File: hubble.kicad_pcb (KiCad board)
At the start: 4 copper layers, 60 x 80 mm, 97 parts, among them J1 USB3_A_LCSC, J2 USB3_A_LCSC, J3 USB_C_Receptacle_Molex, J5 USB3_A_LCSC, J6 USB3_A_LCSC, J7 USB3_A_LCSC, J8 USB3_A_LCSC, J9 Conn_02x02_Odd_Even, SW1 K3-2235D-F1, U1 MAX6816EUS+T, U10 TPD1E05U06DPY, U11 TPD1E05U06DPY, U12 TPD1E05U06DPY, U13 TPD1E05U06DPY, U2 TPD1E05U06DPY, U3 TS3USB221RSER, U4 TPS7A5201QRGRRQ1, U5 USB5744, U6 TPS7A5201QRGRRQ1, U7 FUSB340, U8 TPD1E05U06DPY, U9 TPD1E05U06DPY, Y1 X322525MOB4SI

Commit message: Add ki-lime-pi-to-go submodule, upgrade to KiCad 9, put a Pico W and through hole header on the schematic
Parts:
- added A1: RaspberryPi_Pico_W, Module_RaspberryPi_Pico:RaspberryPi_Pico_Common_THT, F.Cu at (70.1, 74.4)
- added J10: Pico_Socket_B, Module_RaspberryPi_Pico:RaspberryPi_Pico_PinSocket_1x20_P2.54mm_Vertical, F.Cu at (97.0, 97.5)
- added J4: Pico_Socket_A, Module_RaspberryPi_Pico:RaspberryPi_Pico_PinSocket_1x20_P2.54mm_Vertical, F.Cu at (35.9, 51.1)

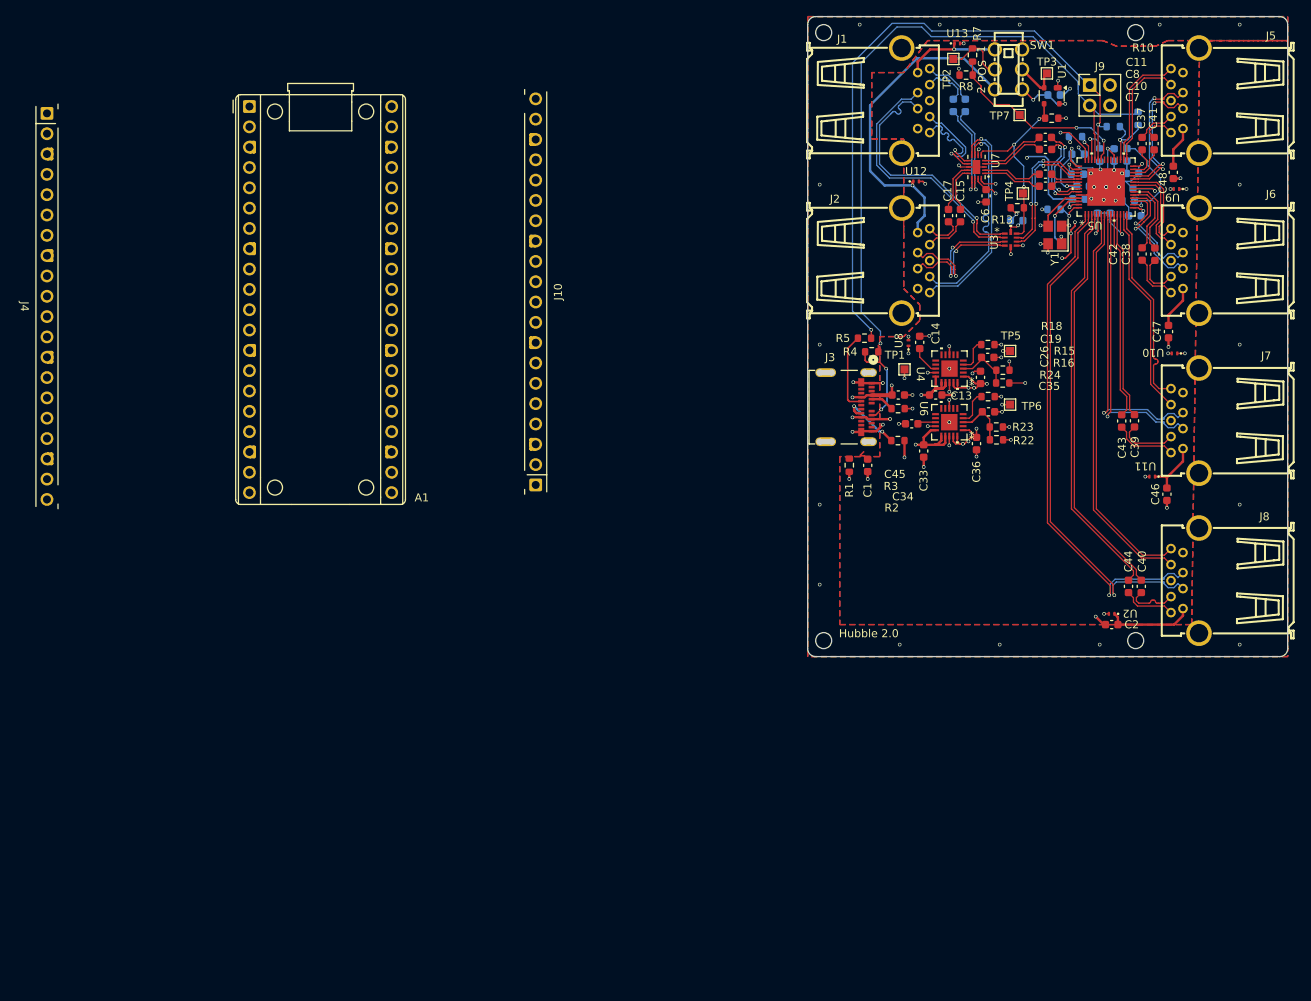
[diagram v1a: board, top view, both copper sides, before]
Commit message: Start wiring up Pi Pico
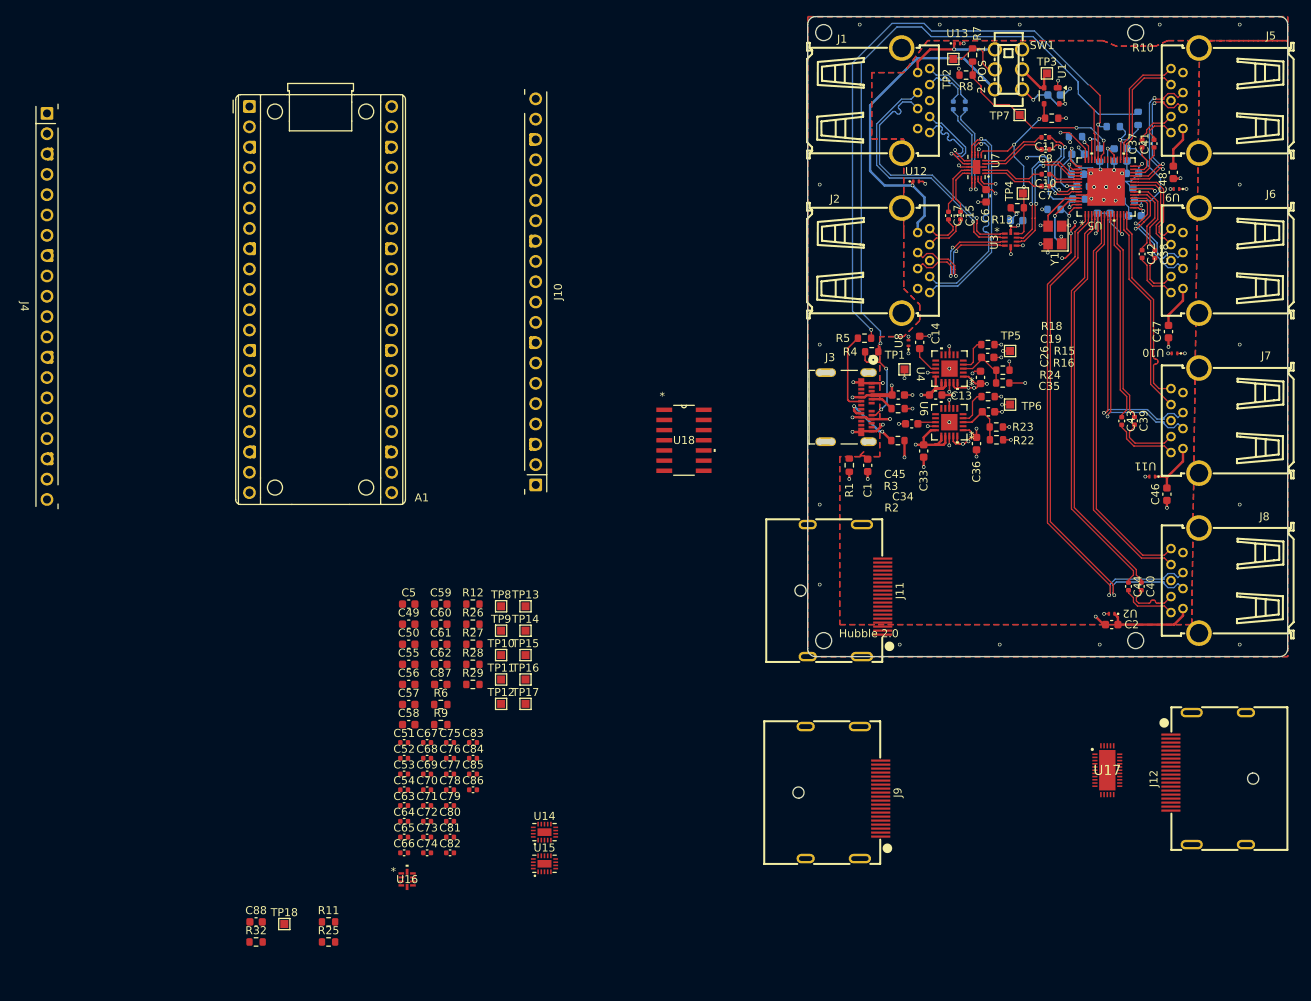
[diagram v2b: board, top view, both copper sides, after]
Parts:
- added C49: 0.1uF, Capacitor_SMD:C_0603_1608Metric, F.Cu at (81.1, 115.0)
- added C5: 0.1uF, Capacitor_SMD:C_0603_1608Metric, F.Cu at (81.1, 112.4)
- added C50: 0.1uF, Capacitor_SMD:C_0603_1608Metric, F.Cu at (81.1, 117.5)
- added C51: 0.1uF, Capacitor_SMD:C_0402_1005Metric, F.Cu at (80.6, 129.7)
- added C52: 0.1uF, Capacitor_SMD:C_0402_1005Metric, F.Cu at (80.6, 131.7)
- added C53: 0.1uF, Capacitor_SMD:C_0402_1005Metric, F.Cu at (80.6, 133.7)
- added C54: 0.1uF, Capacitor_SMD:C_0402_1005Metric, F.Cu at (80.6, 135.7)
- added C55: 0.1uF, Capacitor_SMD:C_0603_1608Metric, F.Cu at (81.1, 120.0)
- added C56: 0.1uF, Capacitor_SMD:C_0603_1608Metric, F.Cu at (81.1, 122.5)
- added C57: 0.1uF, Capacitor_SMD:C_0603_1608Metric, F.Cu at (81.1, 125.0)
- added C58: 0.1uF, Capacitor_SMD:C_0603_1608Metric, F.Cu at (81.1, 127.5)
- added C59: 0.1uF, Capacitor_SMD:C_0603_1608Metric, F.Cu at (85.1, 112.4)
- added C60: 0.1uF, Capacitor_SMD:C_0603_1608Metric, F.Cu at (85.1, 115.0)
- added C61: 0.1uF, Capacitor_SMD:C_0603_1608Metric, F.Cu at (85.1, 117.5)
- added C62: 4.7uF, Capacitor_SMD:C_0603_1608Metric, F.Cu at (85.1, 120.0)
- added C63: 0.1uF, Capacitor_SMD:C_0402_1005Metric, F.Cu at (80.6, 137.6)
- added C64: 0.1uF, Capacitor_SMD:C_0402_1005Metric, F.Cu at (80.6, 139.6)
- added C65: 0.1uF, Capacitor_SMD:C_0402_1005Metric, F.Cu at (80.6, 141.6)
- added C66: 0.1uF, Capacitor_SMD:C_0402_1005Metric, F.Cu at (80.6, 143.5)
- added C67: 0.1uF, Capacitor_SMD:C_0402_1005Metric, F.Cu at (83.4, 129.7)
- added C68: 0.1uF, Capacitor_SMD:C_0402_1005Metric, F.Cu at (83.4, 131.7)
- added C69: 0.1uF, Capacitor_SMD:C_0402_1005Metric, F.Cu at (83.4, 133.7)
- added C70: 0.1uF, Capacitor_SMD:C_0402_1005Metric, F.Cu at (83.4, 135.7)
- added C71: 0.1uF, Capacitor_SMD:C_0402_1005Metric, F.Cu at (83.4, 137.6)
- added C72: 0.1uF, Capacitor_SMD:C_0402_1005Metric, F.Cu at (83.4, 139.6)
- added C73: 0.1uF, Capacitor_SMD:C_0402_1005Metric, F.Cu at (83.4, 141.6)
- added C74: 0.1uF, Capacitor_SMD:C_0402_1005Metric, F.Cu at (83.4, 143.5)
- added C75: 0.1uF, Capacitor_SMD:C_0402_1005Metric, F.Cu at (86.3, 129.7)
- added C76: 0.1uF, Capacitor_SMD:C_0402_1005Metric, F.Cu at (86.3, 131.7)
- added C77: 0.1uF, Capacitor_SMD:C_0402_1005Metric, F.Cu at (86.3, 133.7)
- added C78: 0.1uF, Capacitor_SMD:C_0402_1005Metric, F.Cu at (86.3, 135.7)
- added C79: 0.1uF, Capacitor_SMD:C_0402_1005Metric, F.Cu at (86.3, 137.6)
- added C80: 0.1uF, Capacitor_SMD:C_0402_1005Metric, F.Cu at (86.3, 139.6)
- added C81: 0.1uF, Capacitor_SMD:C_0402_1005Metric, F.Cu at (86.3, 141.6)
- added C82: 0.1uF, Capacitor_SMD:C_0402_1005Metric, F.Cu at (86.3, 143.5)
- added C83: 0.1uF, Capacitor_SMD:C_0402_1005Metric, F.Cu at (89.2, 129.7)
- added C84: 0.1uF, Capacitor_SMD:C_0402_1005Metric, F.Cu at (89.2, 131.7)
- added C85: 0.1uF, Capacitor_SMD:C_0402_1005Metric, F.Cu at (89.2, 133.7)
- added C86: 0.1uF, Capacitor_SMD:C_0402_1005Metric, F.Cu at (89.2, 135.7)
- added C87: 0.1uF, Capacitor_SMD:C_0603_1608Metric, F.Cu at (85.1, 122.5)
- added C88: 0.1uF, Capacitor_SMD:C_0603_1608Metric, F.Cu at (62.0, 152.2)
- added J11: DisplayPort, hubble:DISPLAYPORT_XDPF-0205-20S, F.Cu at (135.7, 110.8)
- added J12: DisplayPort, hubble:DISPLAYPORT_XDPF-0205-20S, F.Cu at (181.1, 134.2)
- added R11: 0, Resistor_SMD:R_0603_1608Metric, F.Cu at (71.1, 152.2)
- added R12: 1M, Resistor_SMD:R_0603_1608Metric, F.Cu at (89.1, 112.4)
- added R25: 0, Resistor_SMD:R_0603_1608Metric, F.Cu at (71.1, 154.7)
- added R26: 10k, Resistor_SMD:R_0603_1608Metric, F.Cu at (89.1, 115.0)
- added R27: 10k, Resistor_SMD:R_0603_1608Metric, F.Cu at (89.1, 117.5)
- added R28: 1M, Resistor_SMD:R_0603_1608Metric, F.Cu at (89.1, 120.0)
- added R29: 330, Resistor_SMD:R_0603_1608Metric, F.Cu at (89.1, 122.5)
- added R32: 10k, Resistor_SMD:R_0603_1608Metric, F.Cu at (62.0, 154.7)
- added R6: 330, Resistor_SMD:R_0603_1608Metric, F.Cu at (85.1, 125.0)
- added R9: 330, Resistor_SMD:R_0603_1608Metric, F.Cu at (85.1, 127.5)
- added TP10: TestPoint, TestPoint:TestPoint_Pad_1.0x1.0mm, F.Cu at (92.7, 118.8)
- added TP11: TestPoint, TestPoint:TestPoint_Pad_1.0x1.0mm, F.Cu at (92.7, 121.9)
- added TP12: TestPoint, TestPoint:TestPoint_Pad_1.0x1.0mm, F.Cu at (92.7, 124.9)
- added TP13: TestPoint, TestPoint:TestPoint_Pad_1.0x1.0mm, F.Cu at (95.7, 112.7)
- added TP14: TestPoint, TestPoint:TestPoint_Pad_1.0x1.0mm, F.Cu at (95.7, 115.8)
- added TP15: TestPoint, TestPoint:TestPoint_Pad_1.0x1.0mm, F.Cu at (95.7, 118.8)
- added TP16: TestPoint, TestPoint:TestPoint_Pad_1.0x1.0mm, F.Cu at (95.7, 121.9)
- added TP17: TestPoint, TestPoint:TestPoint_Pad_1.0x1.0mm, F.Cu at (95.7, 124.9)
- added TP18: TestPoint, TestPoint:TestPoint_Pad_1.0x1.0mm, F.Cu at (65.6, 152.4)
- added TP8: TestPoint, TestPoint:TestPoint_Pad_1.0x1.0mm, F.Cu at (92.7, 112.7)
- added TP9: TestPoint, TestPoint:TestPoint_Pad_1.0x1.0mm, F.Cu at (92.7, 115.8)
- added U14: FUSB340, hubble:TMLP-18_L2.8-W2.0-P0.40-BL-EP, F.Cu at (98.1, 140.9)
- added U15: FUSB340, hubble:TMLP-18_L2.8-W2.0-P0.40-BL-EP, F.Cu at (98.1, 144.9)
- added U16: TS3USB221RSER, hubble:UQFN-10, F.Cu at (80.9, 146.9)
- added U17: PI3DPX1203BZLEX, hubble:QFN40P300X600X80-33N, F.Cu at (168.4, 133.2)
- added U18: SN74CBTLV3126DR, hubble:D14, F.Cu at (115.5, 92.0)
- C10, C11, C15, C16, C17, C18, C37, C38, C39, C40, C41, C42, C43, C44, C7, C8: footprint Capacitor_SMD:C_0603_1608Metric -> Capacitor_SMD:C_0402_1005Metric
- J9: value Conn_02x02_Odd_Even -> DisplayPort; footprint Connector_PinHeader_2.54mm:PinHeader_2x02_P2.54mm_Vertical -> hubble:DISPLAYPORT_XDPF-0205-20S
- moved J9 93.7 mm to (135.4, 136.0), turned to -90 degrees
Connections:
- net /DEVICE_1_USB_N renamed /Hub/DEVICE_1_USB_N
- net /DEVICE_1_USB_P renamed /Hub/DEVICE_1_USB_P
- net /DEVICE_2_USB_N renamed /Hub/DEVICE_2_USB_N
- net /DEVICE_2_USB_P renamed /Hub/DEVICE_2_USB_P
- net /DEVICE_3_USB_N renamed /Hub/DEVICE_3_USB_N
- net /DEVICE_3_USB_P renamed /Hub/DEVICE_3_USB_P
- net /DEVICE_4_USB_N renamed /Hub/DEVICE_4_USB_N
- net /DEVICE_4_USB_P renamed /Hub/DEVICE_4_USB_P
- net /HOST_1_USB_N renamed /Hub/HOST_1_USB_N
- net /HOST_1_USB_P renamed /Hub/HOST_1_USB_P
- net /HOST_2_USB_N renamed /Hub/HOST_2_USB_N
- net /HOST_2_USB_P renamed /Hub/HOST_2_USB_P
- net /HUB_USB_N renamed /Hub/HUB_USB_N
- net /HUB_USB_P renamed /Hub/HUB_USB_P
- net /MUX_SEL renamed /DisplayPort/MUX_SEL
- net /MUX_SEL_PRE renamed /MCU/MUX_SEL_PRE
- net /SS_RX_DEVICE_1_N renamed /Hub/SS_RX_DEVICE_1_N
- net /SS_RX_DEVICE_1_P renamed /Hub/SS_RX_DEVICE_1_P
- net /SS_RX_DEVICE_2_N renamed /Hub/SS_RX_DEVICE_2_N
- net /SS_RX_DEVICE_2_P renamed /Hub/SS_RX_DEVICE_2_P
- net /SS_RX_DEVICE_3_N renamed /Hub/SS_RX_DEVICE_3_N
- net /SS_RX_DEVICE_3_P renamed /Hub/SS_RX_DEVICE_3_P
- net /SS_RX_DEVICE_4_N renamed /Hub/SS_RX_DEVICE_4_N
- net /SS_RX_DEVICE_4_P renamed /Hub/SS_RX_DEVICE_4_P
- net /SS_RX_HOST_1_N renamed /Hub/SS_RX_HOST_1_N
- net /SS_RX_HOST_1_P renamed /Hub/SS_RX_HOST_1_P
- net /SS_RX_HOST_2_N renamed /Hub/SS_RX_HOST_2_N
- net /SS_RX_HOST_2_P renamed /Hub/SS_RX_HOST_2_P
- net /SS_TX_DEVICE_1_CAP_N renamed /Hub/SS_TX_DEVICE_1_CAP_N
- net /SS_TX_DEVICE_1_CAP_P renamed /Hub/SS_TX_DEVICE_1_CAP_P
- net /SS_TX_DEVICE_1_N renamed /Hub/SS_TX_DEVICE_1_N
- net /SS_TX_DEVICE_1_P renamed /Hub/SS_TX_DEVICE_1_P
- net /SS_TX_DEVICE_2_CAP_N renamed /Hub/SS_TX_DEVICE_2_CAP_N
- net /SS_TX_DEVICE_2_CAP_P renamed /Hub/SS_TX_DEVICE_2_CAP_P
- net /SS_TX_DEVICE_2_N renamed /Hub/SS_TX_DEVICE_2_N
- net /SS_TX_DEVICE_2_P renamed /Hub/SS_TX_DEVICE_2_P
- net /SS_TX_DEVICE_3_CAP_N renamed /Hub/SS_TX_DEVICE_3_CAP_N
- net /SS_TX_DEVICE_3_CAP_P renamed /Hub/SS_TX_DEVICE_3_CAP_P
- net /SS_TX_DEVICE_3_N renamed /Hub/SS_TX_DEVICE_3_N
- net /SS_TX_DEVICE_3_P renamed /Hub/SS_TX_DEVICE_3_P
- net /SS_TX_DEVICE_4_CAP_N renamed /Hub/SS_TX_DEVICE_4_CAP_N
- net /SS_TX_DEVICE_4_CAP_P renamed /Hub/SS_TX_DEVICE_4_CAP_P
- net /SS_TX_DEVICE_4_N renamed /Hub/SS_TX_DEVICE_4_N
- net /SS_TX_DEVICE_4_P renamed /Hub/SS_TX_DEVICE_4_P
- net /VBUS_DET renamed /Hub/VBUS_DET
- net /VBUS_DET_1 renamed /Hub/VBUS_DET_1
- net /VBUS_DET_2 renamed /Hub/VBUS_DET_2
- C10 pad 1: /SS_TX_HUB_P -> /Hub/SS_TX_HUB_CAP_P
- C10 pad 2: /SS_TX_HUB_CAP_P -> /Hub/SS_TX_HUB_P
- C11 pad 1: /SS_RX_HUB_P -> /Hub/SS_TX_HUB_CAP_N
- C11 pad 2: /SS_RX_HUB_CAP_P -> /Hub/SS_TX_HUB_N
- C15 pad 1: /SS_TX_HOST_2_CAP_N -> /Hub/SS_TX_HOST_1_P
- C15 pad 2: /SS_TX_HOST_2_N -> /Hub/SS_TX_HOST_1_CAP_P
- C16 pad 1: /SS_TX_HOST_1_CAP_N -> /Hub/SS_TX_HOST_1_N
- C16 pad 2: /SS_TX_HOST_1_N -> /Hub/SS_TX_HOST_1_CAP_N
- C17 pad 1: /SS_TX_HOST_2_CAP_P -> /Hub/SS_TX_HOST_2_N
- C17 pad 2: /SS_TX_HOST_2_P -> /Hub/SS_TX_HOST_2_CAP_N
- C18 pad 1: /SS_TX_HOST_1_CAP_P -> /Hub/SS_TX_HOST_2_P
- C18 pad 2: /SS_TX_HOST_1_P -> /Hub/SS_TX_HOST_2_CAP_P
- C7 pad 1: /SS_TX_HUB_N -> /Hub/SS_RX_HUB_CAP_P
- C7 pad 2: /SS_TX_HUB_CAP_N -> /Hub/SS_RX_HUB_P
- C8 pad 1: /SS_RX_HUB_N -> /Hub/SS_RX_HUB_CAP_N
- C8 pad 2: /SS_RX_HUB_CAP_N -> /Hub/SS_RX_HUB_N
- J1 pad 8: /SS_TX_HOST_1_N -> /Hub/SS_TX_HOST_1_N
- J1 pad 9: /SS_TX_HOST_1_P -> /Hub/SS_TX_HOST_1_P
- J2 pad 8: /SS_TX_HOST_2_N -> /Hub/SS_TX_HOST_2_N
- J2 pad 9: /SS_TX_HOST_2_P -> /Hub/SS_TX_HOST_2_P
- J9 pad 1: /I2C_SCL -> /DisplayPort/DP_HOST0_D0_P
- J9 pad 3: /I2C_SDA -> /DisplayPort/DP_HOST0_D0_N
- J9 pad 4: unconnected-(J9-Pin_4-Pad4) -> /DisplayPort/DP_HOST0_D1_P
- R14 pad 2: /I2C_SDA -> /DisplayPort/I2C_SCL
- R17 pad 2: /I2C_SCL -> /DisplayPort/I2C_SDA
- R4 pad 2: /I2C_SDA -> /DisplayPort/I2C_SDA
- R5 pad 2: /I2C_SCL -> /DisplayPort/I2C_SCL
- U5 pad 38: /I2C_SCL -> Net-(U5-SPI_CLK/SMCLK)
- U5 pad 39: /I2C_SDA -> Net-(U5-SPI_DO/SMDAT)
- U5 pad 47: /SS_TX_HUB_P -> /Hub/SS_TX_HUB_P
- U5 pad 48: /SS_TX_HUB_N -> /Hub/SS_TX_HUB_N
- U5 pad 50: /SS_RX_HUB_P -> /Hub/SS_RX_HUB_P
- U5 pad 51: /SS_RX_HUB_N -> /Hub/SS_RX_HUB_N
- U7 pad 1: /SS_TX_HUB_CAP_N -> /Hub/SS_TX_HUB_CAP_N
- U7 pad 13: /SS_TX_HOST_2_CAP_P -> /Hub/SS_TX_HOST_2_CAP_P
- U7 pad 14: /SS_TX_HOST_2_CAP_N -> /Hub/SS_TX_HOST_2_CAP_N
- U7 pad 15: /SS_TX_HOST_1_CAP_N -> /Hub/SS_TX_HOST_1_CAP_N
- U7 pad 16: /SS_TX_HOST_1_CAP_P -> /Hub/SS_TX_HOST_1_CAP_P
- U7 pad 2: /SS_TX_HUB_CAP_P -> /Hub/SS_TX_HUB_CAP_P
- U7 pad 4: /SS_RX_HUB_CAP_N -> /Hub/SS_RX_HUB_CAP_N
- U7 pad 5: /SS_RX_HUB_CAP_P -> /Hub/SS_RX_HUB_CAP_P
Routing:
- net /I2C_SCL: track 81.2 -> 11.2 mm, vias 2 -> 1
- net /DisplayPort/I2C_SCL: track 0.00 -> 70.1 mm, vias 0 -> 1
- net Net-(U5-SPI_DO/SMDAT): track 0.00 -> 7.07 mm
- net /I2C_SDA: track 87.2 -> 80.2 mm

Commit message: Wire up more of the Pico
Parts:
- added D1: LED_green, LED_SMD:LED_0603_1608Metric, F.Cu at (42.4, 123.6)
- added D2: LED_green, LED_SMD:LED_0603_1608Metric, F.Cu at (42.4, 126.2)
- added R18: 10k, Resistor_SMD:R_0603_1608Metric, F.Cu at (38.4, 123.6)
- added R24: 330, Resistor_SMD:R_0603_1608Metric, F.Cu at (38.4, 126.1)
- added R30: 10k, Resistor_SMD:R_0603_1608Metric, F.Cu at (38.4, 111.5)
- added R31: 27, Resistor_SMD:R_0603_1608Metric, F.Cu at (38.4, 114.0)
- added R33: 27, Resistor_SMD:R_0603_1608Metric, F.Cu at (38.4, 116.5)
- added R34: 10k, Resistor_SMD:R_0603_1608Metric, F.Cu at (38.4, 128.6)
- added R35: 330, Resistor_SMD:R_0603_1608Metric, F.Cu at (38.4, 131.1)
- added R36: 10k, Resistor_SMD:R_0603_1608Metric, F.Cu at (38.4, 119.1)
- added SW2: K3-2235D-F1, hubble:SW-TH_K3-2235D-F1, F.Cu at (45.6, 113.4)
- added TP19: TestPoint, TestPoint:TestPoint_Pad_1.0x1.0mm, F.Cu at (41.9, 118.1)
- moved J4 16.5 mm to (52.3, 52.6)
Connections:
- J10 pad 1: Net-(A1-GPIO16) -> unconnected-(J10-GPIO16-Pad1)
- J10 pad 10: Net-(A1-RUN) -> /MCU/PI_RUN
- J10 pad 11: Net-(A1-GPIO26_ADC0) -> unconnected-(J10-GPIO26_ADC0-Pad11)
- J10 pad 12: Net-(A1-GPIO27_ADC1) -> unconnected-(J10-GPIO27_ADC1-Pad12)
- J10 pad 13: Net-(A1-AGND) -> GND
- J10 pad 14: Net-(A1-GPIO28_ADC2) -> unconnected-(J10-GPIO28_ADC2-Pad14)
- J10 pad 15: Net-(A1-ADC_VREF) -> unconnected-(J10-ADC_VREF-Pad15)
- J10 pad 16: Net-(A1-3V3) -> unconnected-(J10-3V3-Pad16)
- J10 pad 17: Net-(A1-3V3_EN) -> unconnected-(J10-3V3_EN-Pad17)
- J10 pad 18: Net-(A1-GND-Pad13) -> GND
- J10 pad 19: Net-(A1-VSYS) -> VBUS_IN
- J10 pad 2: Net-(A1-GPIO17) -> unconnected-(J10-GPIO17-Pad2)
- J10 pad 20: Net-(A1-VBUS) -> VBUS_IN
- J10 pad 3: Net-(A1-GND-Pad13) -> GND
- J10 pad 4: Net-(A1-GPIO18) -> unconnected-(J10-GPIO18-Pad4)
- J10 pad 5: Net-(A1-GPIO19) -> unconnected-(J10-GPIO19-Pad5)
- J10 pad 6: Net-(A1-GPIO20) -> unconnected-(J10-GPIO20-Pad6)
- J10 pad 7: Net-(A1-GPIO21) -> unconnected-(J10-GPIO21-Pad7)
- J10 pad 8: Net-(A1-GND-Pad13) -> GND
- J10 pad 9: Net-(A1-GPIO22) -> unconnected-(J10-GPIO22-Pad9)
- J3 pad A6: unconnected-(J3-D+-PadA6) -> /Power/MCU_USB_DP
- J3 pad A7: unconnected-(J3-D--PadA7) -> /Power/MCU_USB_DN
- J3 pad B6: unconnected-(J3-D+-PadB6) -> /Power/MCU_USB_DP
- J3 pad B7: unconnected-(J3-D--PadB7) -> /Power/MCU_USB_DN
- J4 pad 1: Net-(A1-GPIO0) -> /MCU/MUX_SEL_MCU
- J4 pad 10: Net-(A1-GPIO7) -> unconnected-(J4-GPIO7-Pad10)
- J4 pad 11: Net-(A1-GPIO8) -> unconnected-(J4-GPIO8-Pad11)
- J4 pad 12: Net-(A1-GPIO9) -> unconnected-(J4-GPIO9-Pad12)
- J4 pad 13: Net-(A1-GND-Pad13) -> GND
- J4 pad 14: Net-(A1-GPIO10) -> unconnected-(J4-GPIO10-Pad14)
- J4 pad 15: Net-(A1-GPIO11) -> unconnected-(J4-GPIO11-Pad15)
- J4 pad 16: Net-(A1-GPIO12) -> unconnected-(J4-GPIO12-Pad16)
- J4 pad 17: Net-(A1-GPIO13) -> unconnected-(J4-GPIO13-Pad17)
- J4 pad 18: Net-(A1-GND-Pad13) -> GND
- J4 pad 19: Net-(A1-GPIO14) -> unconnected-(J4-GPIO14-Pad19)
- J4 pad 2: Net-(A1-GPIO1) -> /MCU/~{DP_RST}
- J4 pad 20: Net-(A1-GPIO15) -> unconnected-(J4-GPIO15-Pad20)
- J4 pad 3: Net-(A1-GND-Pad13) -> GND
- J4 pad 4: Net-(A1-GPIO2) -> /DisplayPort/I2C_SDA
- J4 pad 5: Net-(A1-GPIO3) -> /DisplayPort/I2C_SCL
- J4 pad 6: Net-(A1-GPIO4) -> unconnected-(J4-GPIO4-Pad6)
- J4 pad 7: Net-(A1-GPIO5) -> unconnected-(J4-GPIO5-Pad7)
- J4 pad 8: Net-(A1-GND-Pad13) -> GND
- J4 pad 9: Net-(A1-GPIO6) -> unconnected-(J4-GPIO6-Pad9)
- SW1 pad 2: /MCU/MUX_SEL_PRE -> /MCU/MUX_SEL_MANUAL
- TP3 pad 1: /MCU/MUX_SEL_PRE -> Net-(U1-IN)
- U1 pad 2: /MCU/MUX_SEL_PRE -> Net-(U1-IN)
- U4 pad 4: Net-(U4-PG) -> Net-(D2-A)
- U6 pad 4: Net-(U6-PG) -> Net-(D1-A)
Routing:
- net (no net): track 0.00 -> 217.7 mm, vias 0 -> 8
- net /I2C_SDA: track 80.2 -> 0.00 mm, vias 1 -> 0
- net /SS_TX_HOST_1_CAP_P: track 12.2 -> 0.00 mm, vias 1 -> 0
- net /SS_TX_HOST_1_CAP_N: track 12.2 -> 0.00 mm, vias 1 -> 0
- net /SS_RX_HUB_P: track 11.3 -> 0.00 mm, vias 2 -> 0
- net /I2C_SCL: track 11.2 -> 0.00 mm, vias 1 -> 0
- net /SS_RX_HUB_N: track 11.1 -> 0.00 mm, vias 2 -> 0
- net /SS_RX_HUB_CAP_N: track 8.08 -> 0.00 mm
- net /SS_RX_HUB_CAP_P: track 8.04 -> 0.00 mm
- net /SS_TX_HUB_CAP_N: track 7.53 -> 0.00 mm
- net /SS_TX_HUB_CAP_P: track 7.53 -> 0.00 mm
- net /SS_TX_HOST_1_P: track 6.55 -> 0.00 mm
- net /SS_TX_HOST_1_N: track 6.51 -> 0.00 mm
- net /SS_TX_HOST_2_CAP_P: track 6.44 -> 0.00 mm
- net /SS_TX_HOST_2_CAP_N: track 5.84 -> 0.00 mm
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- removed copper zone on In2.Cu, net GND
- removed copper zone on B.Cu, net Shield
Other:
- board size 60 x 80 mm -> 60 x 121 mm
